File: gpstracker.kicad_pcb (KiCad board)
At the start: 2 copper layers, 60 parts, among them IC1 SIM808, J1 USB_B_Micro, J2 GS2, J3 47553-0001, J4 CONN_COAXIAL, J5 CONN_COAXIAL, J6 Micro_SD_Card, Q1 DMP1045U, SW1 Reset, U1 MCP73832-5-OT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

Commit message: Component placement
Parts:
- added C15: 0.1uF, Capacitors_SMD:C_0805_HandSoldering, F.Cu at (149.9, 68.6)
- BT1: value Battery_Cell -> External battery
- BT2: value Battery_Cell -> Backup battery
- J2: value GS2 -> Leds; footprint Connectors:GS2 -> Pin_Headers:Pin_Header_Straight_1x02_Pitch2.54mm
- J3, J6, R14, R15, TV1: moved to B.Cu
- moved C12 136.6 mm to (125.7, 43.2), turned to 180 degrees
- moved C13 128.6 mm to (124.5, 38.1), turned to 180 degrees
- moved C10 118.2 mm to (137.2, 38.1), turned to 90 degrees
- moved C11 109.6 mm to (129.5, 38.1)
- moved C14 106.8 mm to (133.3, 39.4), turned to 90 degrees
- moved Q1 105.1 mm to (158.8, 34.3), turned to 180 degrees
- moved C6 99.0 mm to (163.8, 41.9), turned to 270 degrees
- moved J6 98.2 mm to (149.9, 45.7)
- moved D3 97.8 mm to (160.0, 40.6), turned to 180 degrees
- moved R16 97.3 mm to (124.5, 40.6), turned to 180 degrees
- moved R17 97.0 mm to (129.5, 40.6), turned to 180 degrees
- moved C8 92.7 mm to (167.6, 38.1), turned to 180 degrees
- moved ICSP1 91.3 mm to (166.4, 62.2)
- moved BT2 91.2 mm to (176.5, 49.5), turned to 90 degrees
- moved TV1 90.7 mm to (129.5, 36.8)
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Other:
- net class High_Power added: clearance 0.2, trace_width 1, via_dia 0.6, via_drill 0.4
- net class Low_power added: clearance 0.2, trace_width 0.3, via_dia 0.6, via_drill 0.4

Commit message: Started routing
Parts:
- added C16: 100uF, Capacitors_Tantalum_SMD:CP_Tantalum_Case-T_EIA-3528-12_Hand, B.Cu at (247.0, 57.1)
- added C17: 33pF, Capacitors_SMD:C_0805_HandSoldering, B.Cu at (221.0, 67.9)
- added C18: 10pF, Capacitors_SMD:C_0805_HandSoldering, B.Cu at (218.4, 67.9)
- added D1: MMSZ5231BT1G, Diodes_SMD:D_SOD-123, B.Cu at (224.8, 68.6)
- J1: value USB_B_Micro -> Molex 47346-0001
- moved BT2 124.7 mm to (53.3, 68.6)
- moved J3 113.9 mm to (243.8, 94.6)
- moved TV1 111.7 mm to (236.9, 67.9)
- moved J6 86.3 mm to (235.6, 55.2)
- moved R15 85.6 mm to (237.5, 47.0)
- moved R14 84.3 mm to (231.1, 47.0)
- moved R4 49.4 mm to (195.6, 92.7), turned to 0 degrees
- moved ICSP1 48.8 mm to (118.7, 73.0), turned to 90 degrees
- moved J5 48.8 mm to (88.9, 87.0), turned to 270 degrees
- moved R5 46.6 mm to (195.6, 90.2), turned to 0 degrees
- moved C5 46.0 mm to (127.0, 52.1), turned to 180 degrees
- moved C9 45.3 mm to (104.8, 57.8)
- moved IC1 45.2 mm to (89.5, 67.3)
- moved LED3 44.7 mm to (191.8, 91.4)
- moved LED4 44.7 mm to (186.7, 91.4)
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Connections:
- U2 pad 2: /RTC_PWR -> Net-(U2-Pad2)
- U2 pad 23: Net-(U2-Pad23) -> /RTC_PWR
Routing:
- net +3V3: track 0.00 -> 35.1 mm
- net /SCL: track 0.00 -> 28.7 mm
- net VBUS: track 0.00 -> 28.3 mm
- net /WAKE_UP: track 0.00 -> 24.5 mm, vias 0 -> 2
- net /SDA: track 0.00 -> 23.1 mm
- net GND: track 0.00 -> 17.6 mm, vias 0 -> 3
- net Net-(R19-Pad1): track 0.00 -> 14.9 mm, vias 0 -> 2
- net /ARD_RX: track 0.00 -> 14.6 mm, vias 0 -> 2
- net +3V3_FDTI: track 0.00 -> 12.5 mm, vias 0 -> 2
- net Net-(C6-Pad1): track 0.00 -> 12.2 mm
- net Net-(C2-Pad1): track 0.00 -> 9.07 mm
- net /DTR: track 0.00 -> 9.05 mm, vias 0 -> 2
- net Net-(LED7-Pad2): track 0.00 -> 7.30 mm
- net /ARD_TX: track 0.00 -> 7.18 mm
- net Net-(R18-Pad1): track 0.00 -> 7.02 mm
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- added copper zone on B.Cu, net GND
- added copper zone on F.Cu, net GND

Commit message: More routing
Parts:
- added C19: 100uF, Capacitors_SMD:CP_Elec_6.3x7.7, F.Cu at (121.9, 70.5)
- C16: footprint Capacitors_Tantalum_SMD:CP_Tantalum_Case-T_EIA-3528-12_Hand -> Capacitors_SMD:CP_Elec_6.3x7.7; moved to F.Cu
- C17, C18, D1, TV1: moved to F.Cu
- moved J5 98.0 mm to (176.5, 43.2), turned to 0 degrees
- moved C16 79.6 mm to (168.9, 41.9), turned to 0 degrees
- moved J4 75.8 mm to (149.9, 75.6), turned to 180 degrees
- moved IC1 72.9 mm to (161.9, 59.1), turned to 270 degrees
- moved R4 68.5 mm to (141.0, 51.4), turned to 90 degrees
- moved R5 64.9 mm to (143.5, 51.4), turned to 90 degrees
- moved D1 63.8 mm to (170.2, 35.6)
- moved C17 62.4 mm to (167.6, 35.6), turned to 90 degrees
- moved C18 62.4 mm to (165.1, 35.6), turned to 90 degrees
- moved R13 60.4 mm to (161.9, 43.8), turned to 0 degrees
- moved C9 49.6 mm to (152.4, 43.8), turned to 180 degrees
- moved LED4 27.3 mm to (159.4, 91.4), turned to 0 degrees
- moved TV1 23.6 mm to (259.7, 73.7), turned to 90 degrees
- moved LED5 19.8 mm to (159.4, 94.0), turned to 0 degrees
- moved R8 19.7 mm to (169.5, 92.1), turned to 90 degrees
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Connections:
- U2 pad 10: /ARD_HTX -> /ARD_HRX
- U2 pad 9: /ARD_HRX -> /ARD_HTX
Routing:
- net /ARD_HRX: track 0.00 -> 52.7 mm, vias 0 -> 2
- net /ARD_HTX: track 0.00 -> 51.8 mm, vias 0 -> 2
- net +BATT: track 1.08 -> 51.7 mm
- net /ARD_RST: track 2.48 -> 45.6 mm, vias 0 -> 3
- net /SCL: track 28.7 -> 44.9 mm
- net VBUS: track 28.3 -> 43.9 mm, vias 0 -> 3
- net /SDA: track 23.1 -> 38.1 mm
- net Net-(R19-Pad1): track 14.9 -> 0.00 mm, vias 2 -> 0
- net +3V3: track 35.1 -> 46.8 mm
- net GND: track 17.6 -> 28.1 mm, vias 3 -> 5
- net Net-(IC1-Pad13): track 0.00 -> 5.41 mm
- net +2V8: track 0.00 -> 3.51 mm
- net /SIM808_S: track 0.00 -> 3.43 mm, vias 0 -> 1
- net Net-(C9-Pad1): track 0.00 -> 3.35 mm
- net Net-(LED3-Pad2): track 0.00 -> 3.18 mm
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
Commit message: Started redo - FTDI / USB
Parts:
- moved C12 111.0 mm to (124.0, 151.6), turned to 270 degrees
- moved C14 107.0 mm to (129.5, 145.0), turned to 90 degrees
- moved R18 106.7 mm to (135.4, 152.4), turned to 0 degrees
- moved U6 105.8 mm to (128.8, 151.4), turned to 180 degrees
- moved R16 105.7 mm to (124.7, 145.0)
- moved R17 105.7 mm to (127.0, 145.0)
- moved R19 105.4 mm to (135.4, 150.6), turned to 0 degrees
- moved LED6 104.8 mm to (135.4, 154.4), turned to 0 degrees
- moved J1 103.8 mm to (126.0, 136.1)
- moved C13 103.4 mm to (123.4, 141.5)
- moved C11 102.1 mm to (128.3, 141.5), turned to 0 degrees
- moved C10 100.2 mm to (132.3, 144.0), turned to 90 degrees
- moved LED7 96.5 mm to (135.4, 148.6), turned to 0 degrees
- moved J5 91.5 mm to (215.9, 125.7), turned to 270 degrees
- moved J4 83.3 mm to (191.1, 148.0)
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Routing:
- net /ARD_HRX: track 52.7 -> 0.00 mm, vias 2 -> 0
- net /ARD_HTX: track 51.8 -> 0.00 mm, vias 2 -> 0
- net +BATT: track 51.7 -> 0.00 mm
- net +3V3: track 46.8 -> 0.00 mm
- net /ARD_RST: track 45.6 -> 0.00 mm, vias 3 -> 0
- net /SCL: track 44.9 -> 0.00 mm
- net /SDA: track 38.1 -> 0.00 mm
- net GND: track 28.1 -> 0.00 mm, vias 5 -> 0
- net VBUS: track 43.9 -> 19.4 mm, vias 3 -> 0
- net /WAKE_UP: track 24.5 -> 0.00 mm, vias 2 -> 0
- net /ARD_RX: track 14.6 -> 0.00 mm, vias 2 -> 0
- net Net-(C6-Pad1): track 10.7 -> 0.00 mm, vias 2 -> 0
- net Net-(C2-Pad1): track 9.07 -> 0.00 mm
- net /DTR: track 8.66 -> 0.00 mm, vias 2 -> 0
- net +3V3_FDTI: track 12.5 -> 20.1 mm
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
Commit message: Redo - Arduino, Sim & power supply
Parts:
- Q1: footprint TO_SOT_Packages_SMD:TO-252-2 -> TO_SOT_Packages_SMD:SOT-23_Handsoldering
- U1: footprint TO_SOT_Packages_SMD:SOT-23-5 -> TO_SOT_Packages_SMD:SOT-23-5_HandSoldering
- moved C1 166.7 mm to (39.4, 161.5)
- moved C17 165.8 mm to (48.3, 150.6), turned to 180 degrees
- moved R1 164.8 mm to (40.6, 158.0), turned to 180 degrees
- moved D1 164.3 mm to (53.1, 150.9), turned to 0 degrees
- moved LED1 163.7 mm to (41.7, 161.5)
- moved U1 163.2 mm to (45.7, 157.0)
- moved C16 162.7 mm to (54.1, 157.2), turned to 270 degrees
- moved C9 161.5 mm to (57.9, 174.8), turned to 270 degrees
- moved R13 160.1 mm to (56.9, 164.6), turned to 90 degrees
- moved LED2 159.2 mm to (45.5, 164.3), turned to 180 degrees
- moved C18 159.1 mm to (53.1, 148.6), turned to 0 degrees
- moved R2 158.8 mm to (45.5, 162.1), turned to 0 degrees
- moved R3 158.7 mm to (45.5, 160.0), turned to 0 degrees
- moved C3 154.5 mm to (48.3, 148.6)
- moved D3 153.2 mm to (39.4, 154.4), turned to 270 degrees
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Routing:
- net +3V3: track 0.00 -> 18.7 mm
- net +2V8: track 0.00 -> 5.30 mm
- net Net-(IC1-Pad13): track 0.00 -> 3.20 mm
- net Net-(R18-Pad1): track 8.23 -> 8.98 mm

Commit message: All major components are roughly placed
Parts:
- ICSP1: footprint Pin_Headers:Pin_Header_Straight_2x03_Pitch2.54mm -> custom-conn:VASCH3x2
- moved R6 164.9 mm to (36.1, 186.2), turned to 90 degrees
- moved C5 163.2 mm to (34.0, 186.2), turned to 90 degrees
- moved R5 160.3 mm to (30.0, 164.6), turned to 180 degrees
- moved R4 160.0 mm to (30.0, 166.6), turned to 180 degrees
- moved U3 150.0 mm to (23.1, 164.3), turned to 0 degrees
- moved U5 147.9 mm to (24.9, 153.7), turned to 180 degrees
- moved R12 144.3 mm to (33.8, 175.5)
- moved SW1 143.6 mm to (41.9, 186.4), turned to 0 degrees
- moved C7 143.3 mm to (28.2, 160.3), turned to 180 degrees
- moved R11 143.2 mm to (31.8, 158.8)
- moved C4 140.7 mm to (30.0, 162.6), turned to 0 degrees
- moved J2 132.8 mm to (63.4, 191.8)
- moved LED4 132.8 mm to (71.0, 190.5)
- moved R10 132.8 mm to (76.1, 193.0)
- moved R9 132.8 mm to (76.1, 190.5)
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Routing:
- net /ARD_RST: track 0.00 -> 46.6 mm, vias 0 -> 2
- net /SIM808_S: track 0.00 -> 45.1 mm, vias 0 -> 2
- net /SDA: track 0.00 -> 28.0 mm
- net /SCL: track 0.00 -> 26.4 mm, vias 0 -> 2
- net +BATT: track 0.00 -> 26.1 mm
- net /ARD_HRX: track 0.00 -> 23.2 mm
- net /ARD_HTX: track 0.00 -> 22.8 mm
- net /SIM808_P: track 0.00 -> 21.4 mm, vias 0 -> 2
- net /DTR: track 0.00 -> 20.7 mm, vias 0 -> 2
- net /ARD_TX: track 0.00 -> 15.5 mm, vias 0 -> 2
- net +3V3: track 18.7 -> 4.91 mm
- net VBUS: track 19.4 -> 32.6 mm
- net /ARD_MOSI: track 0.00 -> 9.80 mm
- net /ARD_RX: track 0.00 -> 9.00 mm
- net Net-(C6-Pad1): track 0.00 -> 8.18 mm
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
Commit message: Most of the routing is done (missing sdcard)
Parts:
- BT2, TV1: moved to B.Cu
- moved J2 114.8 mm to (152.9, 119.9), turned to 270 degrees
- moved C12 112.4 mm to (119.4, 106.2)
- moved C9 112.3 mm to (146.1, 104.9), turned to 90 degrees
- moved C15 112.0 mm to (124.7, 110.5)
- moved C17 112.0 mm to (137.2, 82.5)
- moved IC1 112.0 mm to (160.8, 94.2)
- moved R12 112.0 mm to (122.7, 107.4)
- moved R3 112.0 mm to (134.6, 91.9)
- moved R5 112.0 mm to (118.9, 96.5)
- moved U4 112.0 mm to (130.0, 81.0)
- moved BT1 112.0 mm to (139.4, 74.2)
- moved C11 112.0 mm to (114.6, 115.1)
- moved C14 112.0 mm to (113.3, 111.5)
- moved C16 112.0 mm to (143.0, 89.2)
- moved C18 112.0 mm to (142.0, 80.5)
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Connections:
- TV1 pad 1: +1V8 -> /SIMRST
- TV1 pad 3: /SIMRST -> +1V8
- TV1 pad 4: /SIMCLK -> Net-(TV1-Pad4)
- TV1 pad 5: /SIMDATA -> /SIMCLK
- TV1 pad 6: Net-(TV1-Pad6) -> /SIMDATA
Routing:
- net +3V3: track 4.91 -> 102.0 mm, vias 0 -> 9
- net /NETWORK_LED: track 0.00 -> 41.9 mm, vias 0 -> 2
- net /SIM808_RI: track 0.00 -> 32.2 mm, vias 0 -> 2
- net VBUS: track 32.6 -> 58.3 mm, vias 0 -> 2
- net /WAKE_UP: track 4.38 -> 29.9 mm, vias 0 -> 2
- net GND: track 0.00 -> 24.8 mm, vias 0 -> 2
- net /SIMCLK: track 0.00 -> 15.8 mm, vias 0 -> 1
- net /RTC_PWR: track 2.38 -> 17.4 mm, vias 0 -> 2
- net /SIM808_S: track 45.1 -> 59.5 mm, vias 2 -> 4
- net +1V8: track 0.00 -> 13.5 mm, vias 0 -> 1
- net /SIMDATA: track 0.00 -> 13.5 mm, vias 0 -> 1
- net /ARD_SCK: track 0.00 -> 12.6 mm, vias 0 -> 1
- net Net-(J2-Pad2): track 0.00 -> 12.3 mm
- net /SIMRST: track 0.00 -> 11.3 mm, vias 0 -> 1
- net /ARD_RST: track 46.6 -> 55.0 mm
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- added copper zone on F.Cu, net +BATT

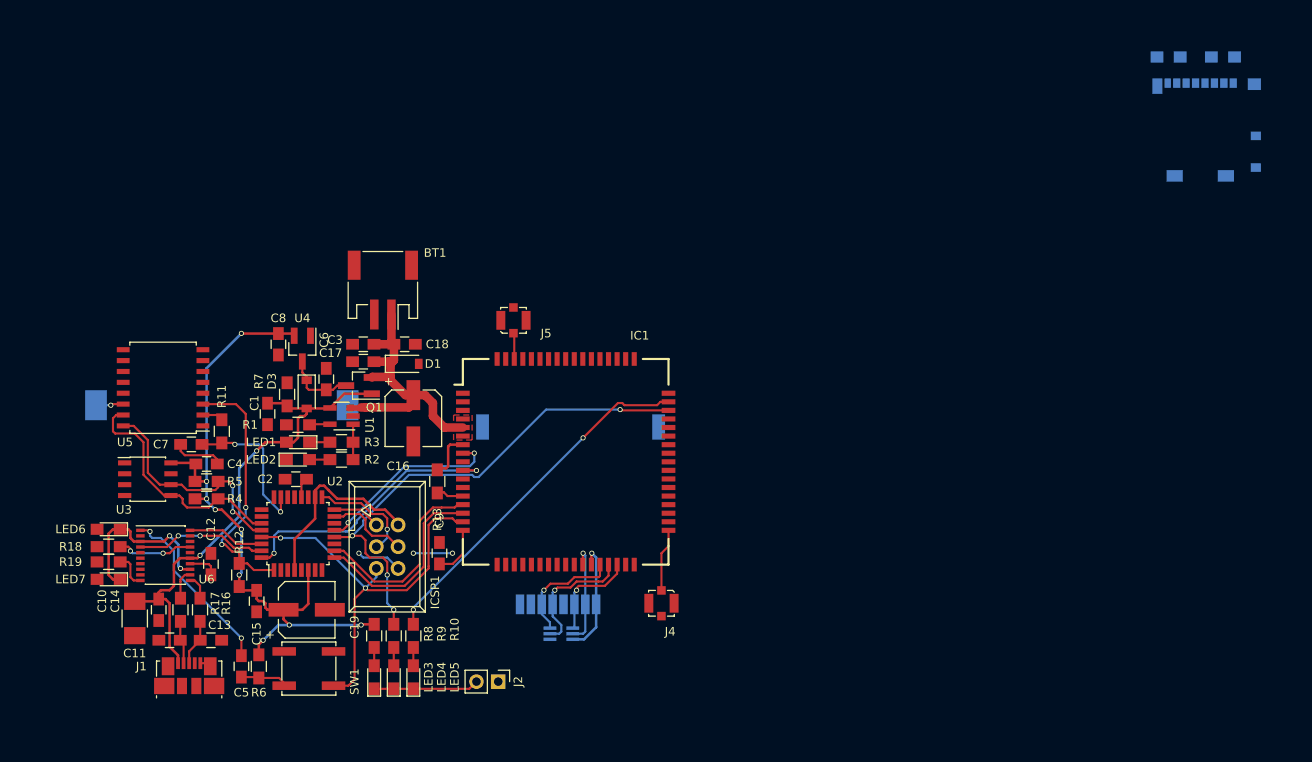
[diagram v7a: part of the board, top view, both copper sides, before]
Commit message: Finsihed routing
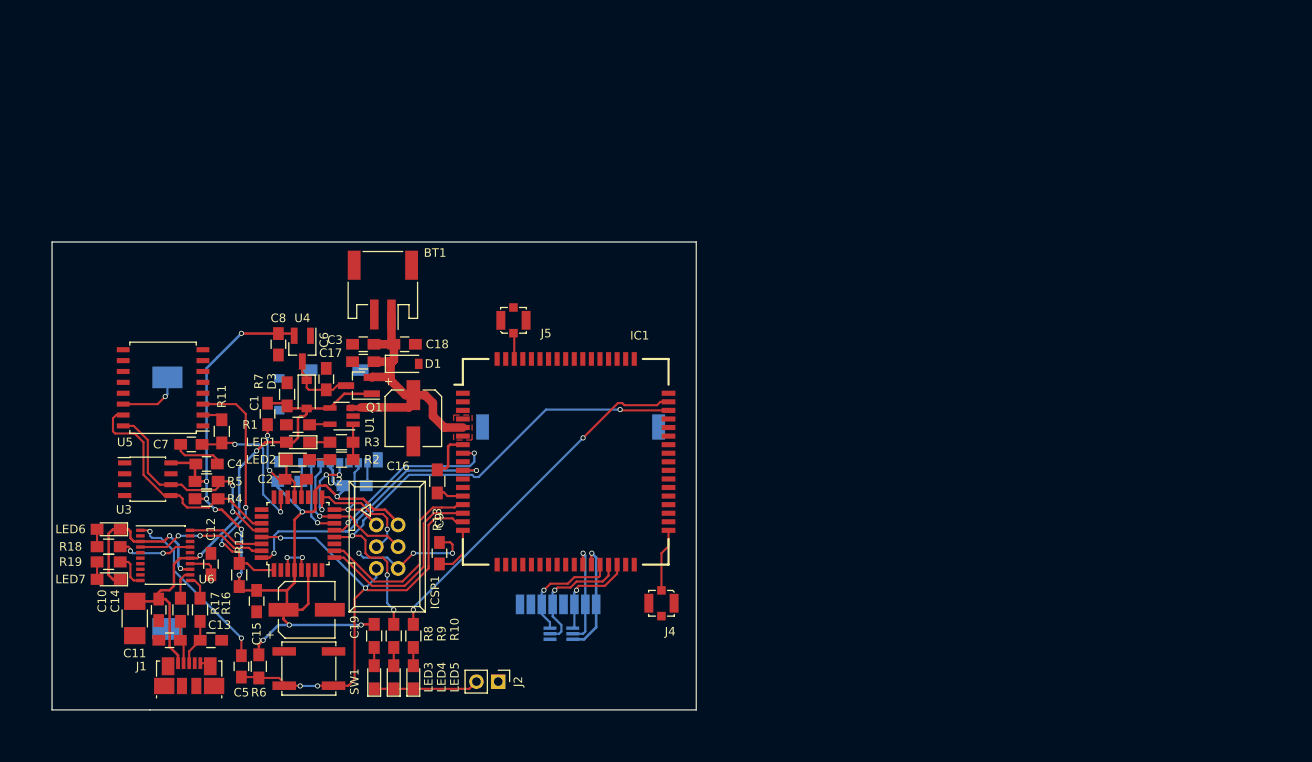
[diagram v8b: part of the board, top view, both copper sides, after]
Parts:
- moved R15 119.7 mm to (128.5, 96.5)
- moved J6 108.0 mm to (133.1, 89.2), turned to 180 degrees
- moved R14 107.4 mm to (136.1, 97.0), turned to 180 degrees
- moved BT2 13.1 mm to (114.3, 99.1), turned to 270 degrees
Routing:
- net GND: track 24.8 -> 52.3 mm, vias 2 -> 8
- net +3V3: track 102.0 -> 116.5 mm, vias 9 -> 11
- net /ARD_IO10: track 0.00 -> 9.29 mm, vias 0 -> 1
- net /ARD_SCK: track 12.6 -> 21.5 mm, vias 1 -> 4
- net /ARD_MOSI: track 9.80 -> 17.5 mm, vias 0 -> 1
- net /ARD_MISO: track 5.63 -> 11.6 mm, vias 0 -> 1
- net /ARD_RST: track 55.0 -> 60.8 mm, vias 2 -> 4
- net (no net): track 4.57 -> 0.00 mm, vias 2 -> 0
- net Net-(BT2-Pad1): track 3.22 -> 7.61 mm
- net Net-(J6-Pad8): track 0.00 -> 2.23 mm
- net Net-(J6-Pad1): track 0.00 -> 2.21 mm
- net Net-(LED7-Pad2): track 0.00 -> 2.03 mm
- net Net-(LED6-Pad2): track 0.00 -> 2.03 mm
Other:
- board outline added: 75.2 x 54.6 mm
